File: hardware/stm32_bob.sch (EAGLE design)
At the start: 52 parts, among them U1 F3_DISCOVERY, U2 LSF0108, U3 INA827, U4 INA827

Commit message: Added values for populated components
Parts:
- added C3, C4: .1u, rcl:C-EUC0805
- C1, C2: value (none) -> .1u
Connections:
- net 3V: now also C4.1
- net 5V: now also C3.1
- net GND: now also C3.2, C4.2
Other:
- note added: "Gain = 5"
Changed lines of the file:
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@@
 <part name="R3" library="rcl" deviceset="R-US_" device="R1206" value="0R"/>
 <part name="R4" library="rcl" deviceset="R-US_" device="R1206" value="0R"/>
-<part name="C1" library="rcl" deviceset="C-EU" device="C0805"/>
-<part name="C2" library="rcl" deviceset="C-EU" device="C0805"/>
+<part name="C1" library="rcl" deviceset="C-EU" device="C0805" value=".1u"/>
+<part name="C2" library="rcl" deviceset="C-EU" device="C0805" value=".1u"/>
 <part name="REF_SEL" library="SparkFun-Connectors" deviceset="M03" device="PTH"/>
 <part name="LVL_EN" library="SparkFun-Connectors" deviceset="M02" device="PTH"/>
@@
 <part name="R28" library="rcl" deviceset="R-US_" device="R0805" value="330"/>
 <part name="R29" library="rcl" deviceset="R-US_" device="R0805" value="330"/>
+<part name="C3" library="rcl" deviceset="C-EU" device="C0805" value=".1u"/>
+<part name="C4" library="rcl" deviceset="C-EU" device="C0805" value=".1u"/>
 </parts>
 <sheets>
@@
 <text x="347.98" y="-63.5" size="2.54" layer="97">LCD Connector</text>
 <text x="345.44" y="-22.86" size="2.54" layer="97">Pushbuttons</text>
+<text x="289.56" y="43.18" size="1.778" layer="97">Gain = 5</text>
+<text x="292.1" y="0" size="1.778" layer="97">Gain = 5</text>
 </plain>
 <instances>
@@
 <instance part="R28" gate="G$1" x="381" y="27.94" rot="R180"/>
 <instance part="R29" gate="G$1" x="381" y="-7.62" rot="R180"/>
+<instance part="C3" gate="G$1" x="259.08" y="124.46"/>
+<instance part="C4" gate="G$1" x="238.76" y="124.46"/>
 </instances>
 <busses>
@@
 <wire x1="347.98" y1="5.08" x2="347.98" y2="-5.08" width="0.1524" layer="91"/>
 <label x="340.36" y="0" size="1.778" layer="95"/>
+</segment>
+<segment>
+<pinref part="C4" gate="G$1" pin="2"/>
+<wire x1="238.76" y1="119.38" x2="238.76" y2="116.84" width="0.1524" layer="91"/>
+<label x="236.22" y="114.3" size="1.778" layer="95"/>
+</segment>
+<segment>
+<pinref part="C3" gate="G$1" pin="2"/>
+<wire x1="259.08" y1="119.38" x2="259.08" y2="116.84" width="0.1524" layer="91"/>
+<label x="256.54" y="114.3" size="1.778" layer="95"/>
 </segment>
 </net>
@@
 <pinref part="R29" gate="G$1" pin="1"/>
 </segment>
+<segment>
+<pinref part="C4" gate="G$1" pin="1"/>
+<wire x1="238.76" y1="127" x2="238.76" y2="129.54" width="0.1524" layer="91"/>
+<label x="238.76" y="129.54" size="1.778" layer="95"/>
+</segment>
 </net>
 <net name="5V" class="0">
@@
 <label x="307.34" y="71.12" size="1.778" layer="95"/>
 </segment>
-</net>
+<segment>
+<pinref part="C3" gate="G$1" pin="1"/>
+<wire x1="259.08" y1="127" x2="259.08" y2="129.54" width="0.1524" layer="91"/>
+<label x="259.08" y="129.54" size="1.778" layer="95"/>
+</segment>
+</net>

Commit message: oops forgot one
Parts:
- R5: value (none) -> 200k
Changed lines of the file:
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@@
 <part name="REF_SEL" library="SparkFun-Connectors" deviceset="M03" device="PTH"/>
 <part name="LVL_EN" library="SparkFun-Connectors" deviceset="M02" device="PTH"/>
-<part name="R5" library="rcl" deviceset="R-US_" device="R0805"/>
+<part name="R5" library="rcl" deviceset="R-US_" device="R0805" value="200k"/>
 <part name="R6" library="rcl" deviceset="R-US_" device="R0805"/>
 <part name="R7" library="rcl" deviceset="R-US_" device="R0805"/>

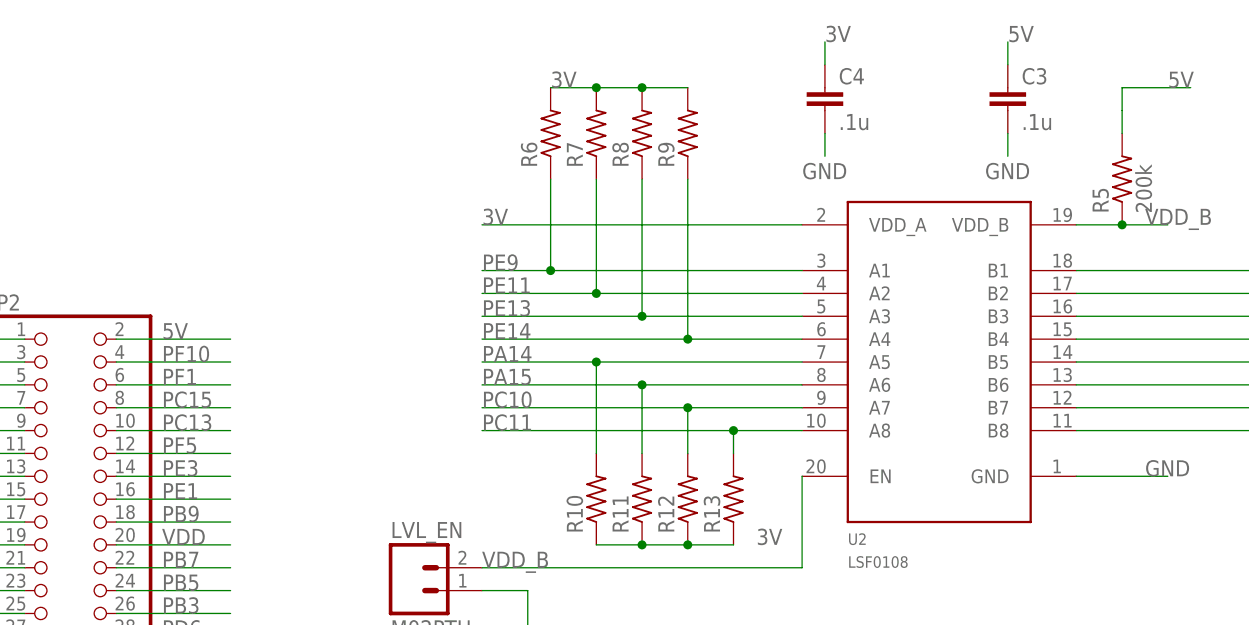
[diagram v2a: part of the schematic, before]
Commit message: Fully routed board
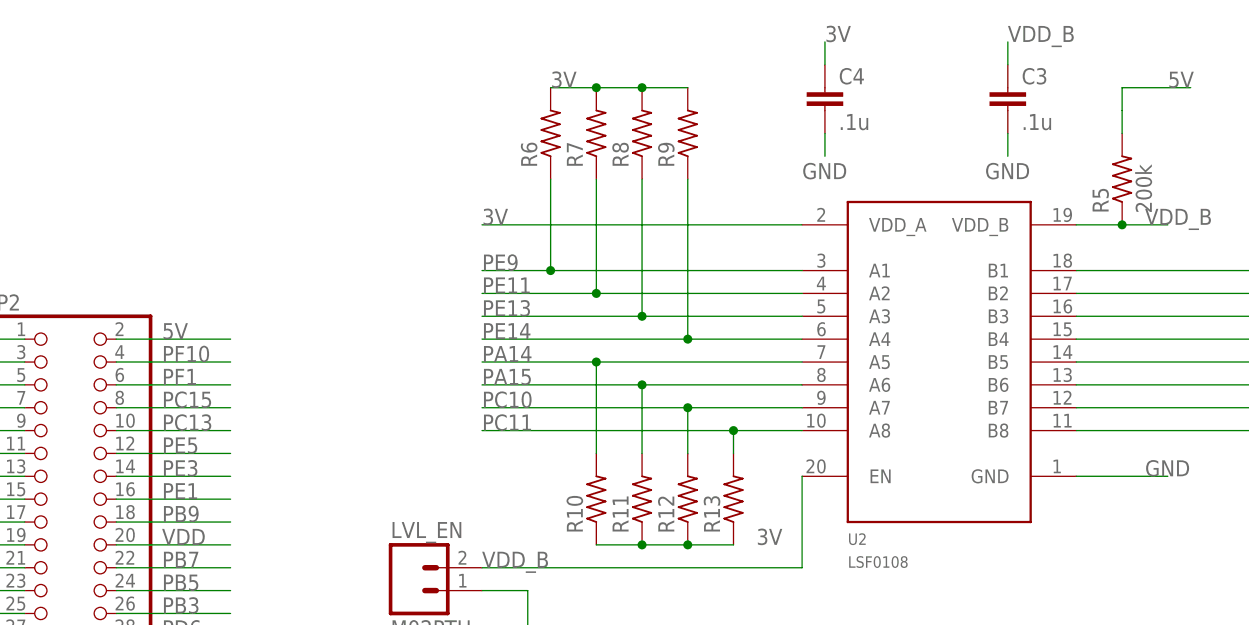
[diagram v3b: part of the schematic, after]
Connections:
- removed net PF5: JP2.12
- net 5V: no longer C3.1
- net PE5: now also JP2.12
- net VDD_B: now also C3.1
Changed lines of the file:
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@@
 <label x="307.34" y="71.12" size="1.778" layer="95"/>
-</segment>
-<segment>
-<pinref part="C3" gate="G$1" pin="1"/>
-<wire x1="259.08" y1="127" x2="259.08" y2="129.54" width="0.1524" layer="91"/>
-<label x="259.08" y="129.54" size="1.778" layer="95"/>
 </segment>
 </net>
@@
 <label x="119.38" y="88.9" size="1.778" layer="95"/>
 </segment>
+<segment>
+<pinref part="JP2" gate="G$1" pin="12"/>
+<wire x1="160.02" y1="83.82" x2="172.72" y2="83.82" width="0.1524" layer="91"/>
+<label x="165.1" y="83.82" size="1.778" layer="95"/>
+</segment>
 </net>
 <net name="PE2" class="0">
@@
 <wire x1="114.3" y1="20.32" x2="121.92" y2="20.32" width="0.1524" layer="91"/>
 <label x="119.38" y="20.32" size="1.778" layer="95"/>
-</segment>
-</net>
-<net name="PF5" class="0">
-<segment>
-<pinref part="JP2" gate="G$1" pin="12"/>
-<wire x1="160.02" y1="83.82" x2="172.72" y2="83.82" width="0.1524" layer="91"/>
-<label x="165.1" y="83.82" size="1.778" layer="95"/>
 </segment>
 </net>
@@
 <label x="200.66" y="71.12" size="1.778" layer="95"/>
 </segment>
-</net>
+<segment>
+<pinref part="C3" gate="G$1" pin="1"/>
+<wire x1="259.08" y1="127" x2="259.08" y2="129.54" width="0.1524" layer="91"/>
+<label x="259.08" y="129.54" size="1.778" layer="95"/>
+</segment>
+</net>
